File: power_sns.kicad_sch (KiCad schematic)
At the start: 2 parts, among them U7 PINA745AIRELR

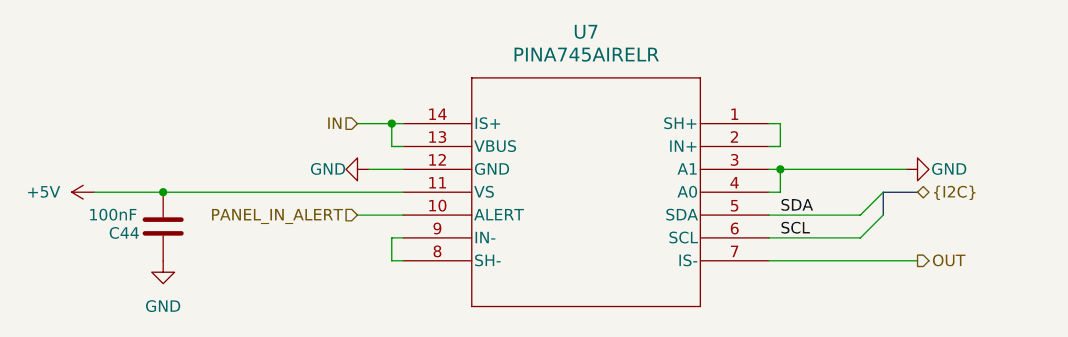
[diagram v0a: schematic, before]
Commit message: Starting bus load switch layout
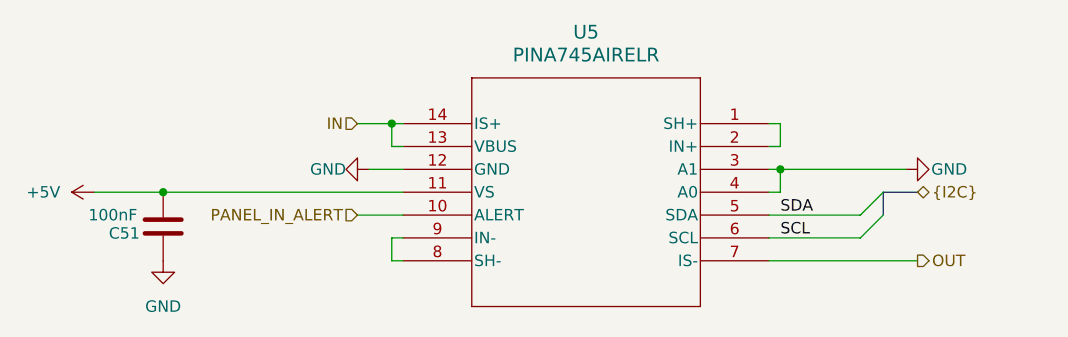
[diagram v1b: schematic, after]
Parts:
- renumbered C44 to C51, U7 to U5
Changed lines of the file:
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@@
 		(on_board yes)
 		(dnp no)
-		(property "Reference" "#PWR054"
+		(property "Reference" "#PWR073"
 			(at 119.38 81.28 0)
 			(effects
@@
 			(project "PowerBoard"
 				(path "/99785679-20de-4827-b4cc-bc3c187068c9/9564929a-642e-4163-88c2-45054b63a5ed/3068c1f6-122c-49ae-9c21-f8ebc0263ff5"
-					(reference "#PWR054")
+					(reference "#PWR073")
 					(unit 1)
 				)
 				(path "/99785679-20de-4827-b4cc-bc3c187068c9/9564929a-642e-4163-88c2-45054b63a5ed/f48ac83e-9a77-49aa-aabc-f4682142862d"
-					(reference "#PWR078")
+					(reference "#PWR082")
 					(unit 1)
 				)
@@
 		(dnp no)
 		(fields_autoplaced yes)
-		(property "Reference" "#PWR053"
+		(property "Reference" "#PWR072"
 			(at 102.87 97.79 0)
 			(effects
@@
 			(project "PowerBoard"
 				(path "/99785679-20de-4827-b4cc-bc3c187068c9/9564929a-642e-4163-88c2-45054b63a5ed/3068c1f6-122c-49ae-9c21-f8ebc0263ff5"
-					(reference "#PWR053")
+					(reference "#PWR072")
 					(unit 1)
 				)
 				(path "/99785679-20de-4827-b4cc-bc3c187068c9/9564929a-642e-4163-88c2-45054b63a5ed/f48ac83e-9a77-49aa-aabc-f4682142862d"
-					(reference "#PWR077")
+					(reference "#PWR081")
 					(unit 1)
 				)
@@
 		(on_board yes)
 		(dnp no)
-		(property "Reference" "U7"
+		(property "Reference" "U5"
 			(at 149.86 66.04 0)
 			(effects
@@
 			(project "PowerBoard"
 				(path "/99785679-20de-4827-b4cc-bc3c187068c9/9564929a-642e-4163-88c2-45054b63a5ed/3068c1f6-122c-49ae-9c21-f8ebc0263ff5"
+					(reference "U5")
+					(unit 1)
+				)
+				(path "/99785679-20de-4827-b4cc-bc3c187068c9/9564929a-642e-4163-88c2-45054b63a5ed/f48ac83e-9a77-49aa-aabc-f4682142862d"
 					(reference "U7")
-					(unit 1)
-				)
-				(path "/99785679-20de-4827-b4cc-bc3c187068c9/9564929a-642e-4163-88c2-45054b63a5ed/f48ac83e-9a77-49aa-aabc-f4682142862d"
-					(reference "U11")
 					(unit 1)
 				)
@@
 		(on_board yes)
 		(dnp no)
-		(property "Reference" "#PWR055"
+		(property "Reference" "#PWR074"
 			(at 191.77 81.28 0)
 			(effects
@@
 			(project "PowerBoard"
 				(path "/99785679-20de-4827-b4cc-bc3c187068c9/9564929a-642e-4163-88c2-45054b63a5ed/3068c1f6-122c-49ae-9c21-f8ebc0263ff5"
-					(reference "#PWR055")
+					(reference "#PWR074")
 					(unit 1)
 				)
 				(path "/99785679-20de-4827-b4cc-bc3c187068c9/9564929a-642e-4163-88c2-45054b63a5ed/f48ac83e-9a77-49aa-aabc-f4682142862d"
-					(reference "#PWR079")
+					(reference "#PWR083")
 					(unit 1)
 				)
@@
 		(on_board yes)
 		(dnp no)
-		(property "Reference" "C44"
+		(property "Reference" "C51"
 			(at 98.552 88.392 0)
 			(effects
@@
 			(project "PowerBoard"
 				(path "/99785679-20de-4827-b4cc-bc3c187068c9/9564929a-642e-4163-88c2-45054b63a5ed/3068c1f6-122c-49ae-9c21-f8ebc0263ff5"
-					(reference "C44")
+					(reference "C51")
 					(unit 1)
 				)
 				(path "/99785679-20de-4827-b4cc-bc3c187068c9/9564929a-642e-4163-88c2-45054b63a5ed/f48ac83e-9a77-49aa-aabc-f4682142862d"
-					(reference "C55")
+					(reference "C54")
 					(unit 1)
 				)
@@
 		(dnp no)
 		(fields_autoplaced yes)
-		(property "Reference" "#PWR052"
+		(property "Reference" "#PWR071"
 			(at 99.06 83.82 0)
 			(effects
@@
 			(project "PowerBoard"
 				(path "/99785679-20de-4827-b4cc-bc3c187068c9/9564929a-642e-4163-88c2-45054b63a5ed/3068c1f6-122c-49ae-9c21-f8ebc0263ff5"
-					(reference "#PWR052")
+					(reference "#PWR071")
 					(unit 1)
 				)
 				(path "/99785679-20de-4827-b4cc-bc3c187068c9/9564929a-642e-4163-88c2-45054b63a5ed/f48ac83e-9a77-49aa-aabc-f4682142862d"
-					(reference "#PWR076")
-					(unit 1)
-				)
+					(reference "#PWR080")
+					(unit 1)
+				)

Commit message: Powerboard planning layout
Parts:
- U5: footprint _Power_Board:REL0014A_PINA745AIRELR_TEX -> _PowerBoard:REL0014A_PINA745AIRELR_TEX
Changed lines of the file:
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@@
 			)
 		)
-		(property "Footprint" "_Power_Board:REL0014A_PINA745AIRELR_TEX"
+		(property "Footprint" "_PowerBoard:REL0014A_PINA745AIRELR_TEX"
 			(at 170.18 76.2 0)
 			(effects

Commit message: Working on schematic and layout
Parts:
- removed U5: PINA745AIRELR, _PowerBoard:REL0014A_PINA745AIRELR_TEX, symbol _INA745:PINA745AIRELR
- added U18: PINA745AIRELR, _PowerBoard:REL0014A_PINA745AIRELR_TEX, symbol _PINA75:PINA745AIRELR
- renumbered C51 to C53
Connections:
- net +5V: now also U18.11 (VS)
- net GND: now also U18.12 (GND), U18.4 (A0)
- net IN: now also U18.13 (VBUS), U18.14 (IS+)
- net OUT: now also U18.7 (IS-)
- net PANEL_IN_ALERT: now also U18.10 (ALERT)
- net SCL: now also U18.6 (SCL)
- net SDA: now also U18.5 (SDA)
- new net: U18.1 (SH+), U18.2 (IN+)
- new net: U18.8 (SH-), U18.9 (IN-)
- new net I2C_SETTING: U18.3 (A1)
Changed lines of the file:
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@@
 		(color 0 0 0 0)
 	)
-	(junction
-		(at 171.45 81.28)
-		(diameter 0)
-		(color 0 0 0 0)
-	)
 	(bus_entry
 		(at 180.34 88.9)
@@
 	(wire
 		(pts
-			(xy 170.18 83.82) (xy 171.45 83.82)
+			(xy 170.18 83.82) (xy 176.53 83.82)
 		)
 		(stroke
@@
 	(wire
 		(pts
-			(xy 129.54 91.44) (xy 128.27 91.44)
+			(xy 176.53 78.74) (xy 185.42 78.74)
 		)
 		(stroke
@@
 	(wire
 		(pts
-			(xy 170.18 76.2) (xy 171.45 76.2)
+			(xy 129.54 91.44) (xy 128.27 91.44)
 		)
 		(stroke
@@
 		)
 	)
-	(bus
+	(wire
 		(pts
-			(xy 182.88 83.82) (xy 182.88 86.36)
+			(xy 179.07 81.28) (xy 184.15 81.28)
 		)
 		(stroke
@@
 	(wire
 		(pts
-			(xy 171.45 81.28) (xy 185.42 81.28)
+			(xy 170.18 76.2) (xy 171.45 76.2)
+		)
+		(stroke
+			(width 0)
+			(type default)
+		)
+	)
+	(bus
+		(pts
+			(xy 182.88 83.82) (xy 182.88 86.36)
 		)
 		(stroke
@@
 	(bus
 		(pts
-			(xy 182.88 83.82) (xy 186.69 83.82)
+			(xy 182.88 83.82) (xy 185.42 83.82)
 		)
 		(stroke
@@
 	(wire
 		(pts
+			(xy 176.53 83.82) (xy 179.07 81.28)
+		)
+		(stroke
+			(width 0)
+			(type default)
+		)
+	)
+	(wire
+		(pts
 			(xy 128.27 76.2) (xy 128.27 78.74)
 		)
@@
 	(wire
 		(pts
-			(xy 125.73 81.28) (xy 129.54 81.28)
+			(xy 172.72 81.28) (xy 176.53 78.74)
 		)
 		(stroke
@@
 	(wire
 		(pts
-			(xy 170.18 78.74) (xy 171.45 78.74)
+			(xy 125.73 81.28) (xy 129.54 81.28)
 		)
 		(stroke
@@
 	(wire
 		(pts
-			(xy 128.27 91.44) (xy 128.27 88.9)
+			(xy 170.18 81.28) (xy 172.72 81.28)
 		)
 		(stroke
@@
 	(wire
 		(pts
-			(xy 170.18 81.28) (xy 171.45 81.28)
+			(xy 170.18 78.74) (xy 171.45 78.74)
 		)
 		(stroke
@@
 	(wire
 		(pts
-			(xy 170.18 88.9) (xy 180.34 88.9)
+			(xy 128.27 91.44) (xy 128.27 88.9)
 		)
 		(stroke
@@
 	(wire
 		(pts
-			(xy 171.45 83.82) (xy 171.45 81.28)
+			(xy 170.18 88.9) (xy 180.34 88.9)
 		)
 		(stroke
@@
 	(wire
 		(pts
-			(xy 170.18 91.44) (xy 186.69 91.44)
+			(xy 170.18 91.44) (xy 185.42 91.44)
 		)
 		(stroke
@@
 	(hierarchical_label "{I2C}"
 		(shape bidirectional)
-		(at 186.69 83.82 0)
+		(at 185.42 83.82 0)
 		(effects
 			(font
@@
 		)
 	)
+	(hierarchical_label "I2C_SETTING"
+		(shape input)
+		(at 185.42 78.74 0)
+		(effects
+			(font
+				(size 1.27 1.27)
+			)
+			(justify left)
+		)
+	)
 	(hierarchical_label "OUT"
 		(shape output)
-		(at 186.69 91.44 0)
+		(at 185.42 91.44 0)
 		(effects
 			(font
@@
 		(on_board yes)
 		(dnp no)
-		(property "Reference" "#PWR073"
+		(property "Reference" "#PWR072"
 			(at 119.38 81.28 0)
 			(effects
@@
 			(project "PowerBoard"
 				(path "/99785679-20de-4827-b4cc-bc3c187068c9/9564929a-642e-4163-88c2-45054b63a5ed/3068c1f6-122c-49ae-9c21-f8ebc0263ff5"
-					(reference "#PWR073")
+					(reference "#PWR072")
 					(unit 1)
 				)
@@
 		(dnp no)
 		(fields_autoplaced yes)
-		(property "Reference" "#PWR072"
+		(property "Reference" "#PWR071"
 			(at 102.87 97.79 0)
 			(effects
@@
 			(project "PowerBoard"
 				(path "/99785679-20de-4827-b4cc-bc3c187068c9/9564929a-642e-4163-88c2-45054b63a5ed/3068c1f6-122c-49ae-9c21-f8ebc0263ff5"
-					(reference "#PWR072")
+					(reference "#PWR071")
 					(unit 1)
 				)
@@
 	)
 	(symbol
-		(lib_id "_INA745:PINA745AIRELR")
+		(lib_id "_PINA75:PINA745AIRELR")
 		(at 170.18 76.2 0)
 		(mirror y)
@@
 		(on_board yes)
 		(dnp no)
-		(property "Reference" "U5"
+		(property "Reference" "U18"
 			(at 149.86 66.04 0)
 			(effects
@@
 			)
 		)
-		(property "Description" "40V, 16BIT HIGH-PRECISION I2C OU"
+		(property "Description" ""
 			(at 170.18 76.2 0)
 			(effects
@@
 			)
 		)
-		(property "Mfr" "Texas Instruments"
+		(property "Mfr" ""
 			(at 170.18 76.2 0)
 			(effects
@@
 			)
 		)
-		(property "Mfr P/N" "INA745AIRELR"
+		(property "Mfr P/N" ""
 			(at 170.18 76.2 0)
 			(effects
@@
 			)
 		)
-		(property "Supplier_1" "Texas Instruments"
+		(property "Supplier_1" ""
 			(at 170.18 76.2 0)
 			(effects
@@
 			)
 		)
-		(property "Supplier_1 P/N" "1"
+		(property "Supplier_1 P/N" ""
 			(at 170.18 76.2 0)
 			(effects
@@
 			)
 		)
-		(property "Supplier_1 Unit Price" "2.044"
+		(property "Supplier_1 Unit Price" ""
 			(at 170.18 76.2 0)
 			(effects
@@
 			)
 		)
-		(property "Supplier_1 Price @ Qty" "1"
+		(property "Supplier_1 Price @ Qty" ""
 			(at 170.18 76.2 0)
 			(effects
@@
 			)
 		)
-		(pin "12"
+		(pin "9"
 		)
-		(pin "1"
+		(pin "10"
 		)
-		(pin "4"
+		(pin "5"
 		)
 		(pin "3"
 		)
-		(pin "2"
+		(pin "1"
 		)
-		(pin "11"
+		(pin "2"
 		)
-		(pin "9"
+		(pin "4"
 		)
-		(pin "10"
+		(pin "14"
 		)
-		(pin "8"
+		(pin "6"
 		)
-		(pin "7"
+		(pin "12"
 		)
-		(pin "14"
+		(pin "13"
 		)
-		(pin "5"
+		(pin "7"
 		)
-		(pin "6"
+		(pin "11"
 		)
-		(pin "13"
+		(pin "8"
 		)
 		(instances
-			(project "PowerBoard"
+			(project ""
 				(path "/99785679-20de-4827-b4cc-bc3c187068c9/9564929a-642e-4163-88c2-45054b63a5ed/3068c1f6-122c-49ae-9c21-f8ebc0263ff5"
-					(reference "U5")
+					(reference "U18")
 					(unit 1)
 				)
 				(path "/99785679-20de-4827-b4cc-bc3c187068c9/9564929a-642e-4163-88c2-45054b63a5ed/f48ac83e-9a77-49aa-aabc-f4682142862d"
-					(reference "U7")
+					(reference "U19")
 					(unit 1)
 				)
@@
 	(symbol
 		(lib_id "power:GND")
-		(at 185.42 81.28 90)
+		(at 184.15 81.28 90)
 		(unit 1)
 		(exclude_from_sim no)
@@
 		(dnp no)
 		(property "Reference" "#PWR074"
-			(at 191.77 81.28 0)
+			(at 190.5 81.28 0)
 			(effects
 				(font
@@
 		)
 		(property "Value" "GND"
-			(at 188.214 81.28 90)
+			(at 186.944 81.28 90)
 			(effects
 				(font
@@
 		)
 		(property "Footprint" ""
-			(at 185.42 81.28 0)
+			(at 184.15 81.28 0)
 			(effects
 				(font
@@
 		)
 		(property "Datasheet" ""
-			(at 185.42 81.28 0)
+			(at 184.15 81.28 0)
 			(effects
 				(font
@@
 		)
 		(property "Description" "Power symbol creates a global label with name \"GND\" , ground"
-			(at 185.42 81.28 0)
+			(at 184.15 81.28 0)
 			(effects
 				(font
@@
 				)
 				(path "/99785679-20de-4827-b4cc-bc3c187068c9/9564929a-642e-4163-88c2-45054b63a5ed/f48ac83e-9a77-49aa-aabc-f4682142862d"
-					(reference "#PWR083")
+					(reference "#PWR084")
 					(unit 1)
 				)
@@
 		(on_board yes)
 		(dnp no)
-		(property "Reference" "C51"
+		(property "Reference" "C53"
 			(at 98.552 88.392 0)
 			(effects
@@
 			(project "PowerBoard"
 				(path "/99785679-20de-4827-b4cc-bc3c187068c9/9564929a-642e-4163-88c2-45054b63a5ed/3068c1f6-122c-49ae-9c21-f8ebc0263ff5"
-					(reference "C51")
+					(reference "C53")
 					(unit 1)
 				)
 				(path "/99785679-20de-4827-b4cc-bc3c187068c9/9564929a-642e-4163-88c2-45054b63a5ed/f48ac83e-9a77-49aa-aabc-f4682142862d"
-					(reference "C54")
+					(reference "C56")
 					(unit 1)
 				)
@@
 		(dnp no)
 		(fields_autoplaced yes)
-		(property "Reference" "#PWR071"
+		(property "Reference" "#PWR070"
 			(at 99.06 83.82 0)
 			(effects
@@
 			(project "PowerBoard"
 				(path "/99785679-20de-4827-b4cc-bc3c187068c9/9564929a-642e-4163-88c2-45054b63a5ed/3068c1f6-122c-49ae-9c21-f8ebc0263ff5"
-					(reference "#PWR071")
+					(reference "#PWR070")
 					(unit 1)
 				)
